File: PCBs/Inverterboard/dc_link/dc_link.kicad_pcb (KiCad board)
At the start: 2 copper layers, 200 x 100.3 mm, 67 parts

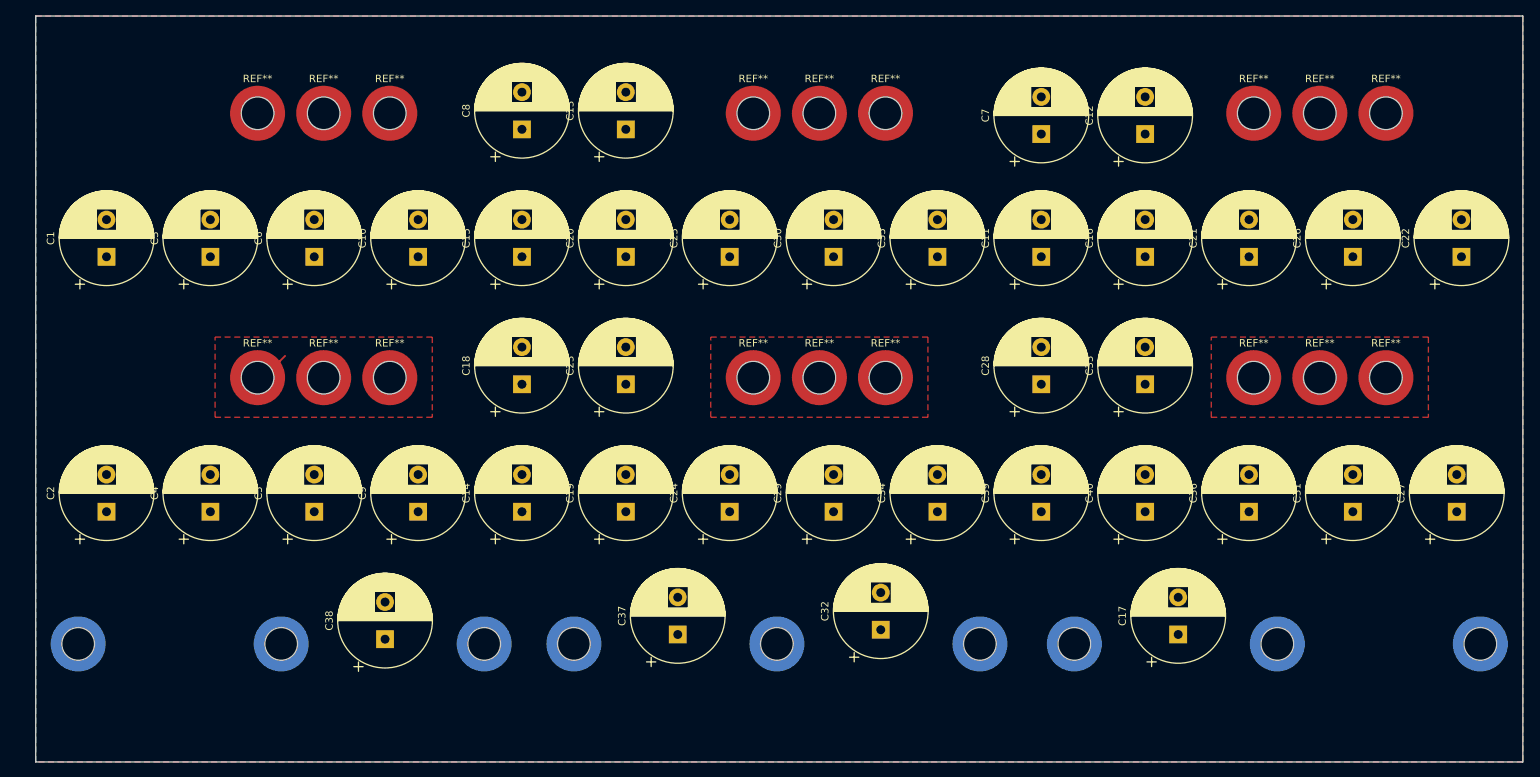
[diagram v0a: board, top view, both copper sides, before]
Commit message: Changed mini-fits to pin headers
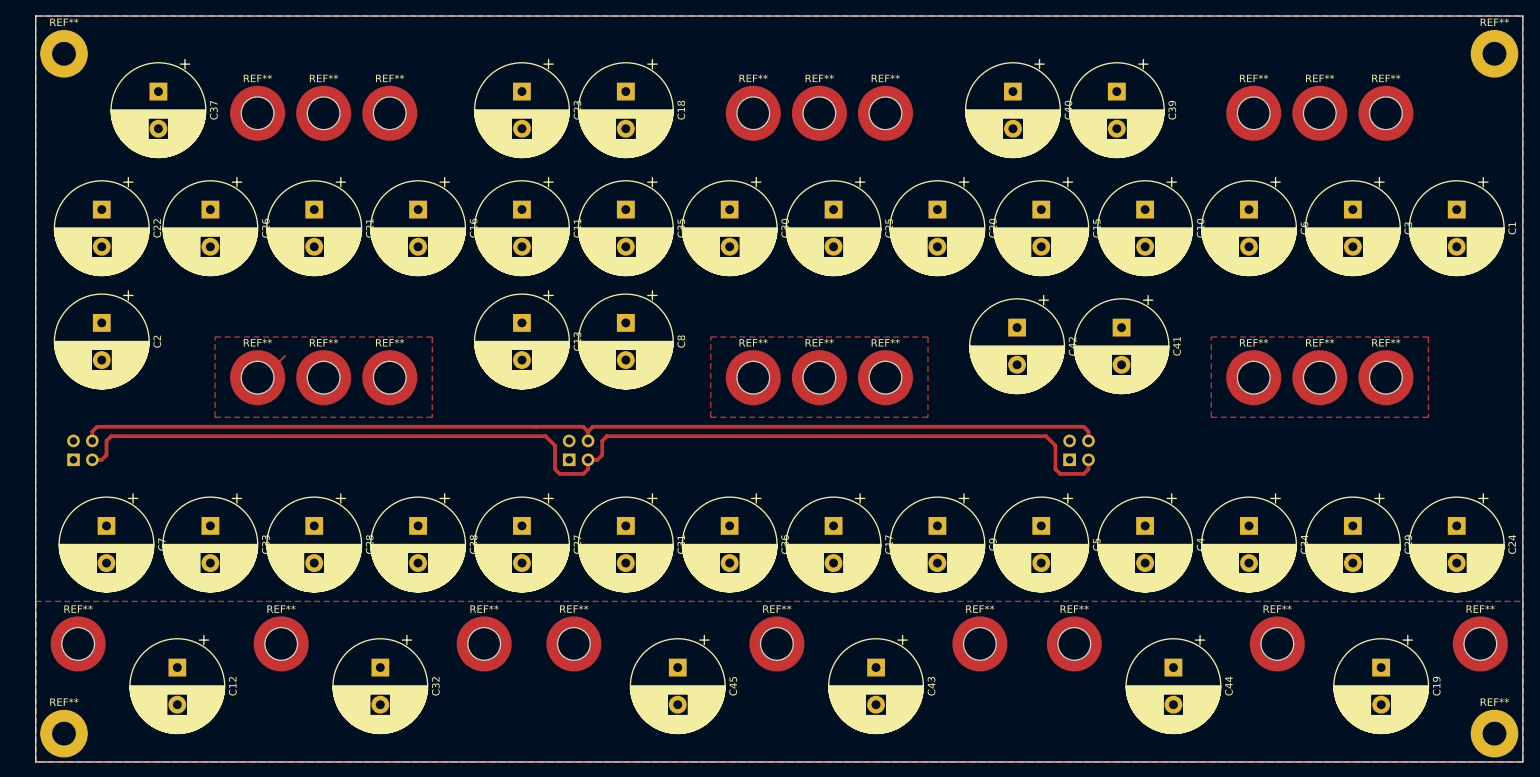
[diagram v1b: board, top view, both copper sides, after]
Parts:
- removed C14: CP, Capacitor_THT:CP_Radial_D12.5mm_P5.00mm
- added C41: CP, Capacitor_THT:CP_Radial_D12.5mm_P5.00mm, F.Cu at (185.4, 80.0)
- added C42: CP, Capacitor_THT:CP_Radial_D12.5mm_P5.00mm, F.Cu at (171.4, 80.0)
- added C43: CP, Capacitor_THT:CP_Radial_D12.5mm_P5.00mm, F.Cu at (152.4, 125.7)
- added C44: CP, Capacitor_THT:CP_Radial_D12.5mm_P5.00mm, F.Cu at (192.4, 125.7)
- added C45: CP, Capacitor_THT:CP_Radial_D12.5mm_P5.00mm, F.Cu at (125.7, 125.7)
- added J2: Conn_02x02_Odd_Even, Connector_PinSocket_2.54mm:PinSocket_2x02_P2.54mm_Vertical, B.Cu at (44.5, 97.8)
- added J3: Conn_02x02_Odd_Even, Connector_PinSocket_2.54mm:PinSocket_2x02_P2.54mm_Vertical, B.Cu at (111.1, 97.8)
- added J4: Conn_02x02_Odd_Even, Connector_PinSocket_2.54mm:PinSocket_2x02_P2.54mm_Vertical, B.Cu at (178.4, 97.8)
- added REF**: MountingHole_3.2mm_M3_Pad, MountingHole:MountingHole_3.2mm_M3_Pad, F.Cu at (43.2, 43.2)
- added REF**: MountingHole_3.2mm_M3_Pad, MountingHole:MountingHole_3.2mm_M3_Pad, F.Cu at (235.6, 43.2)
- added REF**: MountingHole_3.2mm_M3_Pad, MountingHole:MountingHole_3.2mm_M3_Pad, F.Cu at (235.6, 134.6)
- added REF**: MountingHole_3.2mm_M3_Pad, MountingHole:MountingHole_3.2mm_M3_Pad, F.Cu at (43.2, 134.6)
- REF** (x9): moved to F.Cu
- moved C22 183.0 mm to (48.3, 64.1), turned to 270 degrees
- moved C1 181.7 mm to (230.5, 64.1), turned to 270 degrees
- moved C26 153.8 mm to (62.9, 64.1), turned to 270 degrees
- moved C3 153.8 mm to (216.5, 64.1), turned to 270 degrees
- moved C12 148.6 mm to (58.4, 125.7), turned to 270 degrees
- moved C7 136.3 mm to (48.9, 106.7), turned to 270 degrees
- moved C33 127.2 mm to (62.9, 106.7), turned to 270 degrees
- moved C21 125.9 mm to (76.8, 64.1), turned to 270 degrees
- moved C6 125.9 mm to (202.6, 64.1), turned to 270 degrees
- moved C27 125.7 mm to (104.8, 106.7), turned to 270 degrees
- moved C4 125.7 mm to (188.6, 106.7), turned to 270 degrees
- moved C19 103.7 mm to (220.3, 125.7), turned to 270 degrees
- moved C37 101.1 mm to (55.9, 48.3), turned to 270 degrees
- moved C28 99.6 mm to (76.8, 106.7), turned to 270 degrees
- moved C10 98.0 mm to (188.6, 64.1), turned to 270 degrees
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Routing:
- net +12V: track 0.00 -> 149.8 mm
- net +5V: track 0.00 -> 138.8 mm
- added copper zone on F.Cu, net GND

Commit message: Added mini-fit to enable and pwm signals
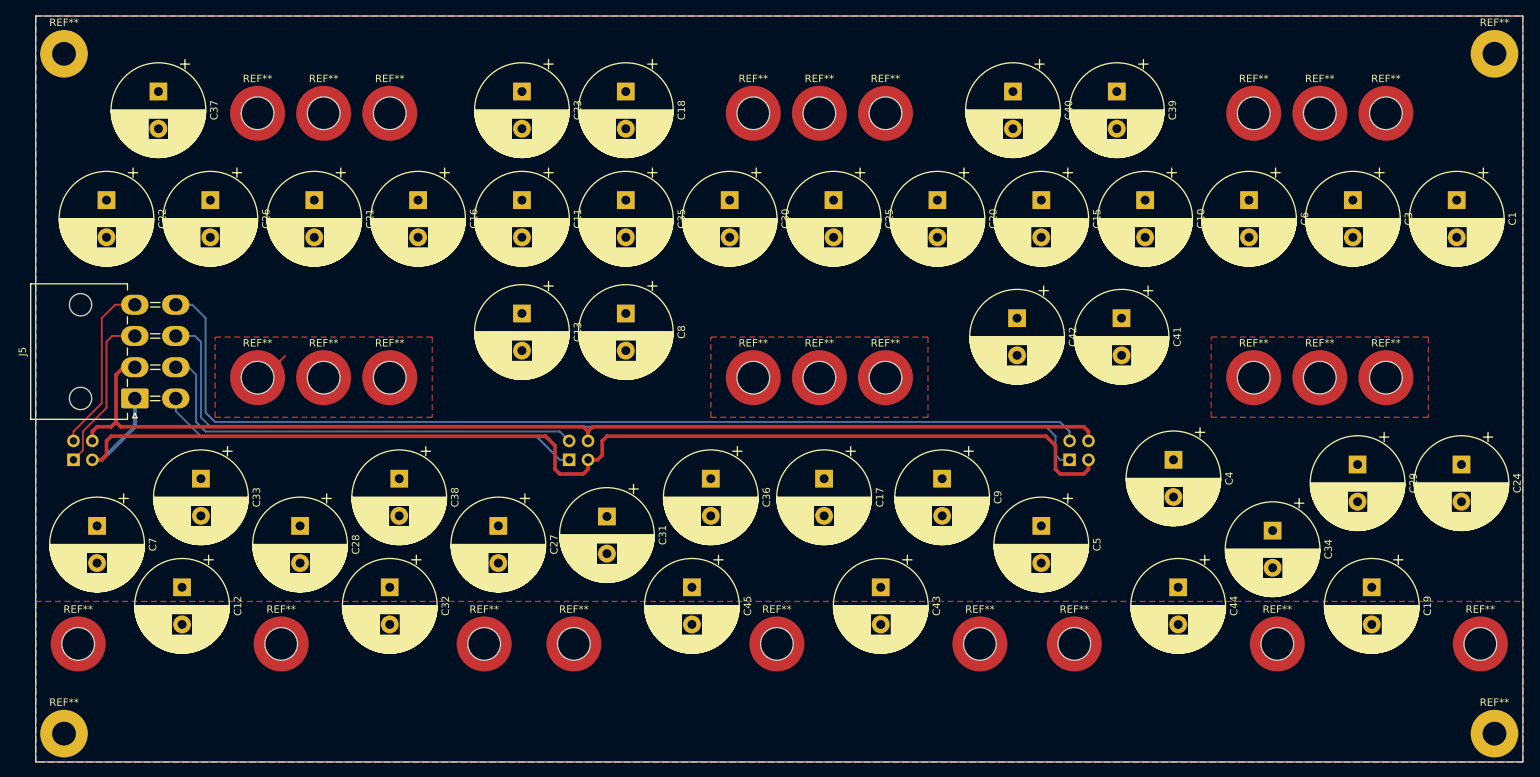
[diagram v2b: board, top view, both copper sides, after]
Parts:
- removed C2: CP, Capacitor_THT:CP_Radial_D12.5mm_P5.00mm
- added J5: Conn_02x04_Odd_Even, Connector_Molex:Molex_Mini-Fit_Jr_5569-08A2_2x04_P4.20mm_Horizontal, F.Cu at (52.7, 89.5)
- moved C45 11.0 mm to (127.6, 114.9)
- moved C19 10.9 mm to (219.1, 114.9)
- moved C32 10.9 mm to (87.0, 114.9)
- moved C12 10.8 mm to (59.1, 114.9)
- moved C43 10.8 mm to (153.0, 114.9)
- moved C44 10.8 mm to (193.0, 114.9)
- moved C4 9.67 mm to (192.4, 97.8)
- moved C24 8.28 mm to (231.1, 98.4)
- moved C29 8.28 mm to (217.2, 98.4)
- moved C38 6.84 mm to (88.3, 100.3)
- moved C36 6.84 mm to (130.2, 100.3)
- moved C17 6.48 mm to (145.4, 100.3)
- moved C33 6.48 mm to (61.6, 100.3)
- moved C9 6.38 mm to (161.3, 100.3)
- moved C34 3.24 mm to (205.7, 107.3)
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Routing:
- net Enable_C: track 0.00 -> 136.0 mm
- net PWM_C: track 0.00 -> 134.6 mm
- net Enable_B: track 0.00 -> 60.7 mm
- net PWM_B: track 0.00 -> 57.3 mm
- net Enable_A: track 0.00 -> 23.3 mm
- net PWM_A: track 0.00 -> 21.8 mm
- net +12V: track 149.8 -> 161.2 mm
- net +5V: track 138.8 -> 148.7 mm

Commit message: Last fixes after PCB review
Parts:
- removed the C21 at (76.8, 62.9)
- removed the C23 at (104.8, 48.3)
- removed the C25 at (146.7, 62.9)
- removed the C27 at (101.6, 106.7)
- removed the C28 at (74.9, 106.7)
- removed C29, C31, C33, C35, C37, C38, C39, C40, C43, C44, C45: CP, Capacitor_THT:CP_Radial_D12.5mm_P5.00mm
- removed J2, J3, J4: Conn_02x02_Odd_Even, Connector_PinSocket_2.54mm:PinSocket_2x02_P2.54mm_Vertical
- removed J5: Conn_02x04_Odd_Even, Connector_Molex:Molex_Mini-Fit_Jr_5569-08A2_2x04_P4.20mm_Horizontal
- removed the REF** at (69.2, 51.2)
- removed the REF** at (45.1, 122.6)
- removed the REF** at (72.4, 122.6)
- removed the REF** at (78.1, 51.2)
- removed the REF** at (99.7, 122.6)
- removed the REF** at (111.8, 122.6)
- removed the REF** at (139.1, 122.6)
- removed the REF** at (166.4, 122.6)
- removed the REF** at (179.1, 122.6)
- removed the REF** at (206.4, 122.6)
- removed the REF** at (233.7, 122.6)
- removed the REF** at (43.2, 43.2)
- removed the REF** at (235.6, 43.2)
- removed the REF** at (235.6, 134.6)
- removed the REF** at (87.0, 51.2)
- removed the REF** at (43.2, 134.6)
- removed the REF** at (221.0, 51.2)
- removed the REF** at (135.9, 51.2)
- removed the REF** at (144.8, 51.2)
- removed the REF** at (153.7, 51.2)
- removed the REF** at (203.2, 51.2)
- removed the REF** at (212.1, 51.2)
- added C24: CP, Capacitor_THT:CP_Radial_D12.5mm_P5.00mm, F.Cu at (104.8, 98.4)
- added REF**: Mounting_Wuerth_WA-SMSR-M3_H2.6mm_ReverseMount_9775026360, Mounting_Wuerth:Mounting_Wuerth_WA-SMSR-M3_H2.6mm_ReverseMount_9775026360, F.Cu at (233.7, 118.7)
- added REF**: Mounting_Wuerth_WA-SMSR-M3_H2.6mm_ReverseMount_9775026360, Mounting_Wuerth:Mounting_Wuerth_WA-SMSR-M3_H2.6mm_ReverseMount_9775026360, F.Cu at (212.1, 56.0)
- added REF**: Mounting_Wuerth_WA-SMSR-M3_H2.6mm_ReverseMount_9775026360, Mounting_Wuerth:Mounting_Wuerth_WA-SMSR-M3_H2.6mm_ReverseMount_9775026360, F.Cu at (203.2, 56.0)
- added REF**: Mounting_Wuerth_WA-SMSR-M3_H2.6mm_ReverseMount_9775026360, Mounting_Wuerth:Mounting_Wuerth_WA-SMSR-M3_H2.6mm_ReverseMount_9775026360, F.Cu at (153.7, 56.0)
- added REF**: Mounting_Wuerth_WA-SMSR-M3_H2.6mm_ReverseMount_9775026360, Mounting_Wuerth:Mounting_Wuerth_WA-SMSR-M3_H2.6mm_ReverseMount_9775026360, F.Cu at (144.8, 56.0)
- added REF**: Mounting_Wuerth_WA-SMSR-M3_H2.6mm_ReverseMount_9775026360, Mounting_Wuerth:Mounting_Wuerth_WA-SMSR-M3_H2.6mm_ReverseMount_9775026360, F.Cu at (135.9, 56.0)
- added REF**: Mounting_Wuerth_WA-SMSR-M3_H2.6mm_ReverseMount_9775026360, Mounting_Wuerth:Mounting_Wuerth_WA-SMSR-M3_H2.6mm_ReverseMount_9775026360, F.Cu at (87.0, 56.0)
- added REF**: Mounting_Wuerth_WA-SMSR-M3_H2.6mm_ReverseMount_9775026360, Mounting_Wuerth:Mounting_Wuerth_WA-SMSR-M3_H2.6mm_ReverseMount_9775026360, F.Cu at (78.1, 56.0)
- added REF**: Mounting_Wuerth_WA-SMSR-M3_H2.6mm_ReverseMount_9775026360, Mounting_Wuerth:Mounting_Wuerth_WA-SMSR-M3_H2.6mm_ReverseMount_9775026360, F.Cu at (206.4, 118.7)
- added REF**: Mounting_Wuerth_WA-SMSR-M3_H2.6mm_ReverseMount_9775026360, Mounting_Wuerth:Mounting_Wuerth_WA-SMSR-M3_H2.6mm_ReverseMount_9775026360, F.Cu at (45.1, 118.7)
- added REF**: Mounting_Wuerth_WA-SMSR-M3_H2.6mm_ReverseMount_9775026360, Mounting_Wuerth:Mounting_Wuerth_WA-SMSR-M3_H2.6mm_ReverseMount_9775026360, F.Cu at (69.2, 56.0)
- added REF**: Mounting_Wuerth_WA-SMSR-M3_H2.6mm_ReverseMount_9775026360, Mounting_Wuerth:Mounting_Wuerth_WA-SMSR-M3_H2.6mm_ReverseMount_9775026360, F.Cu at (179.1, 118.7)
- added REF**: Mounting_Wuerth_WA-SMSR-M3_H2.6mm_ReverseMount_9775026360, Mounting_Wuerth:Mounting_Wuerth_WA-SMSR-M3_H2.6mm_ReverseMount_9775026360, F.Cu at (166.4, 118.7)
- added REF**: Mounting_Wuerth_WA-SMSR-M3_H2.6mm_ReverseMount_9775026360, Mounting_Wuerth:Mounting_Wuerth_WA-SMSR-M3_H2.6mm_ReverseMount_9775026360, F.Cu at (139.1, 118.7)
- added REF**: Mounting_Wuerth_WA-SMSR-M3_H2.6mm_ReverseMount_9775026360, Mounting_Wuerth:Mounting_Wuerth_WA-SMSR-M3_H2.6mm_ReverseMount_9775026360, F.Cu at (111.8, 118.7)
- added REF**: Mounting_Wuerth_WA-SMSR-M3_H2.6mm_ReverseMount_9775026360, Mounting_Wuerth:Mounting_Wuerth_WA-SMSR-M3_H2.6mm_ReverseMount_9775026360, F.Cu at (99.7, 118.7)
- added REF**: Mounting_Wuerth_WA-SMSR-M3_H2.6mm_ReverseMount_9775026360, Mounting_Wuerth:Mounting_Wuerth_WA-SMSR-M3_H2.6mm_ReverseMount_9775026360, F.Cu at (72.4, 118.7)
- added REF**: Mounting_Wuerth_WA-SMSR-M3_H2.6mm_ReverseMount_9775026360, Mounting_Wuerth:Mounting_Wuerth_WA-SMSR-M3_H2.6mm_ReverseMount_9775026360, F.Cu at (221.0, 56.0)
- moved C14 137.9 mm to (48.9, 98.4)
- moved C2 110.3 mm to (62.9, 98.4)
- moved C18 45.2 mm to (77.5, 66.7)
- moved C12 35.8 mm to (90.8, 98.4)
- moved C26 35.8 mm to (118.7, 98.4)
- moved C8 30.8 mm to (147.3, 66.7)
- moved C7 30.4 mm to (76.8, 98.4)
- moved C13 18.5 mm to (119.4, 66.7)
- moved C19 16.6 mm to (217.2, 98.4)
- moved C27 9.25 mm to (203.2, 98.4)
- moved C5 8.28 mm to (175.3, 98.4)
- moved C21 3.86 mm to (49.5, 66.7)
- moved C23 3.86 mm to (63.5, 66.7)
- moved C1 3.86 mm to (231.1, 66.7)
- moved C10 3.86 mm to (189.2, 66.7)
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- renumbered C41 to C14, C42 to C2, C22 to C21, C24 to C22, C26 to C23, C30 to C25, C32 to C26, C34 to C27, C36 to C28
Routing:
- net +12V: track 161.2 -> 0.00 mm
- net +5V: track 148.7 -> 0.00 mm
- net Enable_C: track 136.0 -> 0.00 mm
- net PWM_C: track 134.6 -> 0.00 mm
- net +BATT: track 0.00 -> 109.6 mm
- net Enable_B: track 60.7 -> 0.00 mm
- net PWM_B: track 57.3 -> 0.00 mm
- net Enable_A: track 23.3 -> 0.00 mm
- net PWM_A: track 21.8 -> 0.00 mm
- net PHASE_A: track 3.22 -> 0.00 mm
- net GND: vias 0 -> 146
- added copper zone on B.Cu, net PHASE_A
- added copper zone on B.Cu, net PHASE_B
- added copper zone on B.Cu, net PHASE_C
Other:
- board size 200 x 100.3 mm -> 200 x 71.9 mm

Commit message: Created gerber files
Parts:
- removed the REF** at (87.0, 56.0)
- removed the REF** at (135.9, 86.7)
- removed the REF** at (69.2, 56.0)
- added REF**: Mounting_Wuerth_WA-SMSR-M3_H2.6mm_ReverseMount_9775026360, Mounting_Wuerth:Mounting_Wuerth_WA-SMSR-M3_H2.6mm_ReverseMount_9775026360, F.Cu at (85.6, 56.0)
- added REF**: Mounting_Wuerth_WA-SMSR-M3_H2.6mm_ReverseMount_9775026360, Mounting_Wuerth:Mounting_Wuerth_WA-SMSR-M3_H2.6mm_ReverseMount_9775026360, F.Cu at (134.6, 86.7)
- added REF**: Mounting_Wuerth_WA-SMSR-M3_H2.6mm_ReverseMount_9775026360, Mounting_Wuerth:Mounting_Wuerth_WA-SMSR-M3_H2.6mm_ReverseMount_9775026360, F.Cu at (65.3, 56.0)
- moved REF** 3.94 mm to (199.3, 56.0)
- moved REF** 3.94 mm to (132.0, 56.0)
- moved REF** 2.67 mm to (209.4, 56.0)
- moved REF** 2.67 mm to (142.1, 56.0)
- moved REF** 2.67 mm to (75.4, 56.0)
- moved REF** 1.40 mm to (152.3, 56.0)
- moved REF** 1.40 mm to (219.6, 56.0)
- moved REF** 1.27 mm to (67.9, 86.7)
- moved REF** 1.27 mm to (154.9, 86.7)
- moved REF** 1.27 mm to (222.2, 86.7)
- moved REF** 1.27 mm to (88.3, 86.7)
- moved REF** 1.27 mm to (201.9, 86.7)
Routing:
- net +BATT: track 109.6 -> 126.6 mm
- net GND: vias 146 -> 138
